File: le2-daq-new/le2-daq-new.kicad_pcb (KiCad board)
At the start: 2 copper layers, 161.3 x 88.4 mm, 11 parts, among them J1 PCIE_CONN, J2 PCIE_CONN, J3 PCIE_CONN, J4 PCIE_CONN, J5 Conn_01x02_Male, J6 TEST-POINT, J7 TEST-POINT, SW1 EN_HIGH, U1 ESP32-DEVKITC-32D

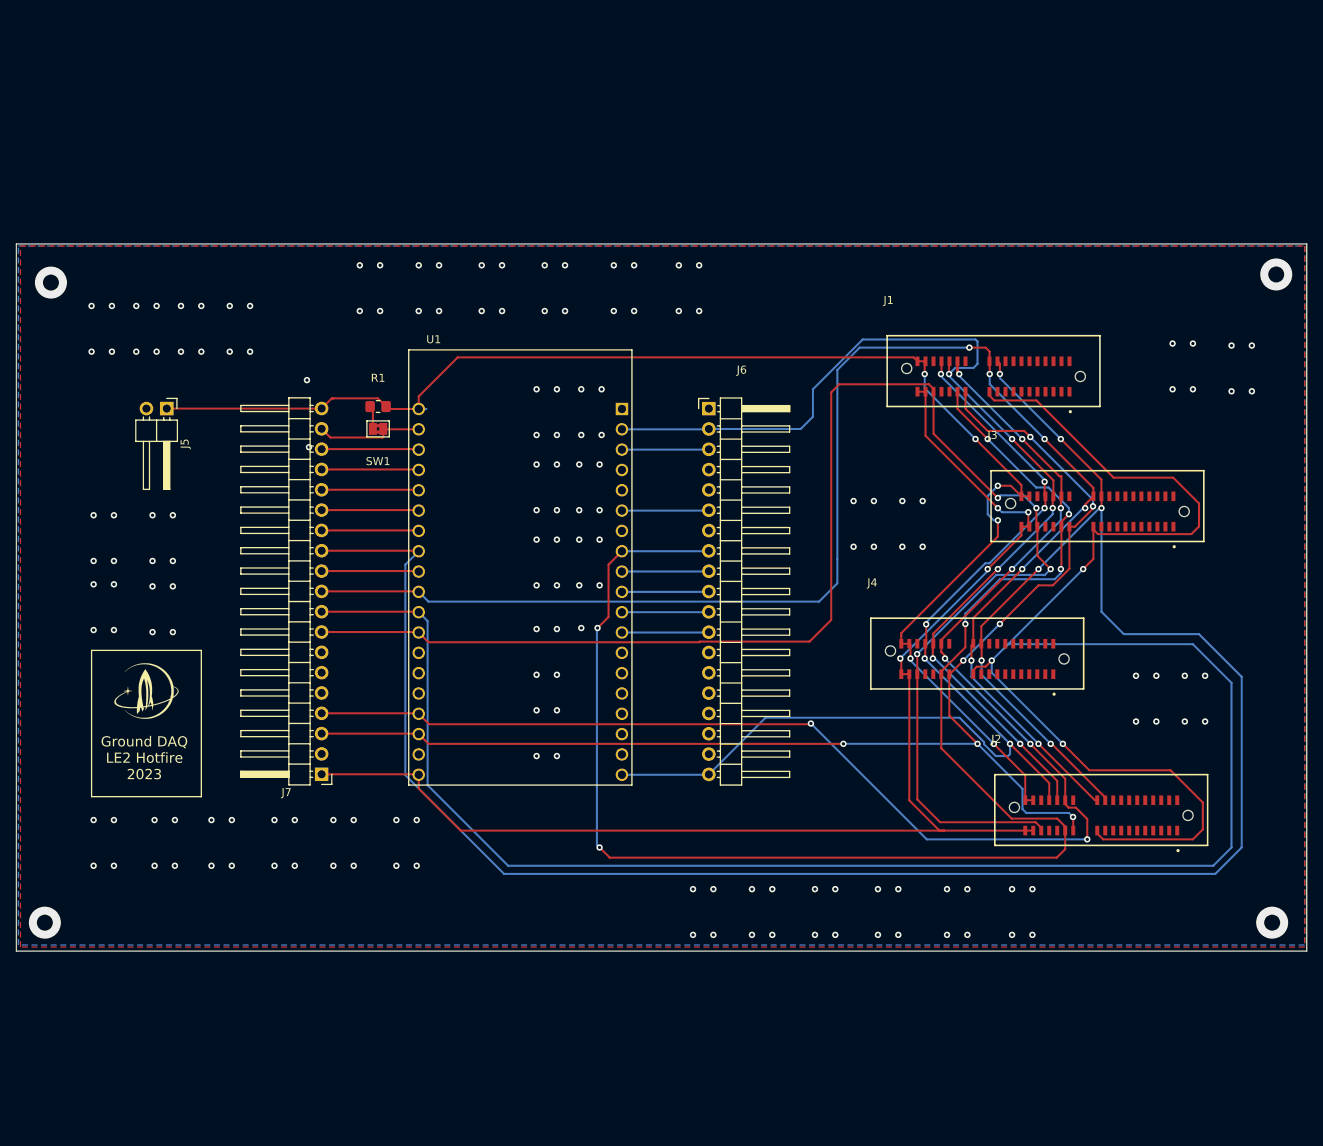
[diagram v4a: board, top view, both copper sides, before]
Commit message: new daq layout
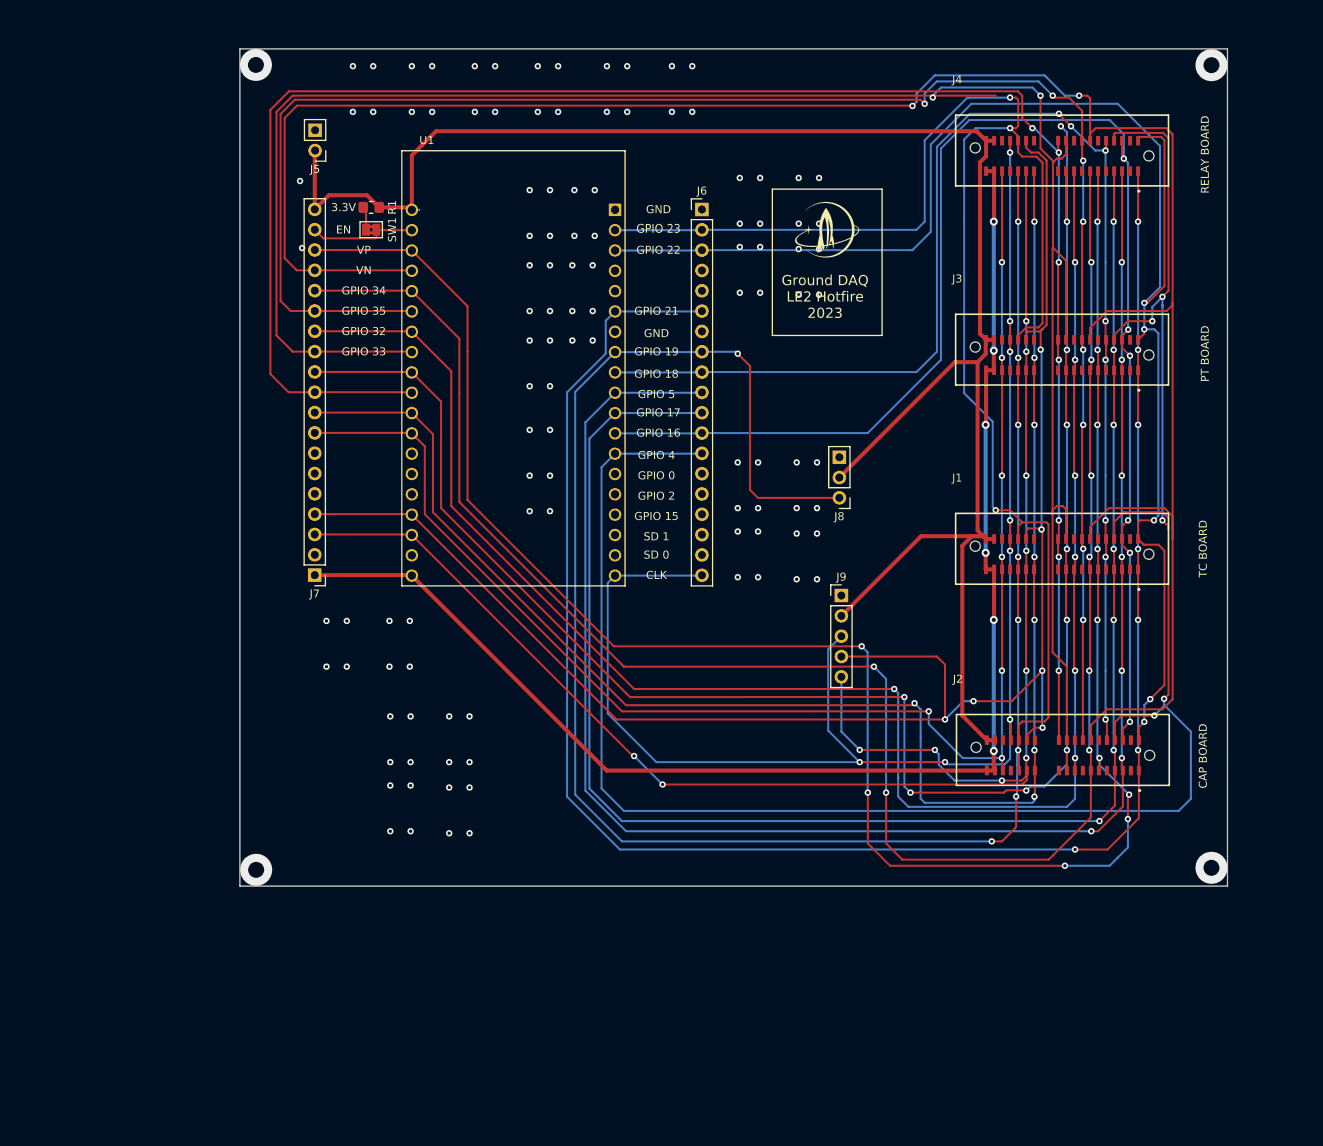
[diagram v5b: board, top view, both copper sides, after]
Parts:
- added J8: Conn_01x03_Male, Connector_PinHeader_2.54mm:PinHeader_1x03_P2.54mm_Vertical, F.Cu at (157.0, 89.4)
- added J9: Conn_01x05_Male, Connector_PinHeader_2.54mm:PinHeader_1x05_P2.54mm_Vertical, F.Cu at (157.2, 101.6)
- J5: value Conn_01x02_Male -> POWER; footprint Connector_PinHeader_2.54mm:PinHeader_1x02_P2.54mm_Horizontal -> Connector_PinHeader_2.54mm:PinHeader_1x02_P2.54mm_Vertical
- J6, J7: footprint Connector_PinHeader_2.54mm:PinHeader_1x19_P2.54mm_Horizontal -> Connector_PinHeader_2.54mm:PinHeader_1x19_P2.54mm_Vertical
- SW1: value EN_HIGH -> SW_Push
- moved G*** 102.8 mm to (155.4, 55.9)
- moved J4 63.8 mm to (184.8, 46.6)
- moved J5 37.2 mm to (91.4, 46.0), turned to 180 degrees
- moved J6 24.9 mm to (139.8, 53.4)
- moved SW1 24.9 mm to (98.5, 55.9)
- moved J7 24.9 mm to (91.4, 99.0)
- moved R1 24.9 mm to (98.5, 53.1)
- moved U1 24.9 mm to (116.2, 73.2)
- moved J1 23.8 mm to (184.8, 96.4)
- moved J3 20.1 mm to (184.8, 71.5)
- moved J2 8.91 mm to (184.9, 121.6)
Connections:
- J1 pad A01: (no net) -> RL SDA
- J1 pad A02: (no net) -> GND
- J1 pad A03: (no net) -> TC SDO
- J1 pad A04: (no net) -> TC SDI
- J1 pad A05: (no net) -> GND
- J1 pad A06: (no net) -> HX 1
- J1 pad A07: (no net) -> HX 3
- J1 pad A08: (no net) -> GND
- J1 pad A09: (no net) -> HX 5
- J1 pad A10: GND -> HX 7
- J1 pad A11: HX CLK -> GND
- J1 pad A12: CAP 2 -> HX CLK
- J1 pad A13: PHOTORES -> CAP 2
- J1 pad A14: GND -> PHOTORES
- J1 pad B01: (no net) -> RL SCL
- J1 pad B02: (no net) -> GND
- J1 pad B03: (no net) -> TC1 CS
- J1 pad B04: (no net) -> TC2 CS
- J1 pad B05: (no net) -> TC CLK
- J1 pad B06: (no net) -> GND
- J1 pad B07: (no net) -> HX 2
- J1 pad B08: (no net) -> HX 4
- J1 pad B09: (no net) -> GND
- J2 pad A01: (no net) -> RL SDA
- J2 pad A02: (no net) -> GND
- J2 pad A03: (no net) -> TC SDO
- J2 pad A04: (no net) -> TC SDI
- J2 pad A05: (no net) -> GND
- J2 pad A06: (no net) -> HX 1
- J2 pad A07: (no net) -> HX 3
- J2 pad A08: (no net) -> GND
- J2 pad A09: (no net) -> HX 5
- J2 pad A10: GND -> HX 7
- J2 pad A11: HX CLK -> GND
- J2 pad A12: CAP 2 -> HX CLK
- J2 pad A13: PHOTORES -> CAP 2
- J2 pad A14: GND -> PHOTORES
- J2 pad B01: (no net) -> RL SCL
- J2 pad B02: (no net) -> GND
- J2 pad B03: (no net) -> TC1 CS
- J2 pad B04: (no net) -> TC2 CS
- J2 pad B05: (no net) -> TC CLK
- J2 pad B06: (no net) -> GND
- J2 pad B07: (no net) -> HX 2
- J2 pad B08: (no net) -> HX 4
- J2 pad B09: (no net) -> GND
- J3 pad A01: (no net) -> RL SDA
- J3 pad A02: (no net) -> GND
- J3 pad A03: (no net) -> TC SDO
- J3 pad A04: (no net) -> TC SDI
- J3 pad A05: (no net) -> GND
- J3 pad A06: (no net) -> HX 1
- J3 pad A07: (no net) -> HX 3
- J3 pad A08: (no net) -> GND
- J3 pad A09: (no net) -> HX 5
- J3 pad A10: GND -> HX 7
- J3 pad A11: HX CLK -> GND
- J3 pad A12: CAP 2 -> HX CLK
- J3 pad A13: PHOTORES -> CAP 2
- J3 pad A14: GND -> PHOTORES
- J3 pad B01: (no net) -> RL SCL
- J3 pad B02: (no net) -> GND
- J3 pad B03: (no net) -> TC1 CS
- J3 pad B04: (no net) -> TC2 CS
- J3 pad B05: (no net) -> TC CLK
- J3 pad B06: (no net) -> GND
- J3 pad B07: (no net) -> HX 2
- J3 pad B08: (no net) -> HX 4
- J3 pad B09: (no net) -> GND
- J4 pad A01: (no net) -> RL SDA
- J4 pad A02: (no net) -> GND
- J4 pad A03: (no net) -> TC SDO
- J4 pad A04: (no net) -> TC SDI
- J4 pad A05: (no net) -> GND
- J4 pad A06: (no net) -> HX 1
- J4 pad A07: (no net) -> HX 3
- J4 pad A08: (no net) -> GND
- J4 pad A09: (no net) -> HX 5
- J4 pad A10: GND -> HX 7
- J4 pad A11: HX CLK -> GND
- J4 pad A12: CAP 2 -> HX CLK
- J4 pad A13: PHOTORES -> CAP 2
- J4 pad A14: GND -> PHOTORES
- J4 pad B01: (no net) -> RL SCL
- J4 pad B02: (no net) -> GND
- J4 pad B03: (no net) -> TC1 CS
- J4 pad B04: (no net) -> TC2 CS
- J4 pad B05: (no net) -> TC CLK
- J4 pad B06: (no net) -> GND
- J4 pad B07: (no net) -> HX 2
- J4 pad B08: (no net) -> HX 4
- J4 pad B09: (no net) -> GND
- J6 pad 10: TC1 CS -> TC SDO
- J6 pad 11: TC SDO -> TC SDI
- J6 pad 12: TC CLK -> TC1 CS
- J6 pad 13: unconnected-(J6-Pad13) -> TC2 CS
- J6 pad 9: TC2 CS -> TC CLK
- U1 pad 28: TC2 CS -> TC CLK
- U1 pad 29: TC1 CS -> TC SDO
- U1 pad 30: TC SDO -> TC SDI
- U1 pad 31: TC CLK -> TC1 CS
- U1 pad 32: unconnected-(U1-Pad32) -> TC2 CS
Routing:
- net HX 2: track 12.2 -> 269.2 mm, vias 0 -> 2
- net TC2 CS: track 10.9 -> 252.0 mm, vias 0 -> 5
- net HX 1: track 12.2 -> 250.7 mm, vias 0 -> 11
- net HX 3: track 12.2 -> 233.9 mm, vias 0 -> 8
- net RL SDA: track 10.9 -> 230.8 mm, vias 0 -> 7
- net HX 4: track 12.2 -> 223.9 mm, vias 0 -> 8
- net HX 7: track 12.2 -> 220.8 mm, vias 0 -> 10
- net TC SDI: track 0.00 -> 206.9 mm, vias 0 -> 7
- net HX 5: track 12.2 -> 218.1 mm, vias 0 -> 7
- net TC SDO: track 10.9 -> 212.3 mm, vias 0 -> 7
- net RL SCL: track 10.9 -> 193.8 mm, vias 0 -> 5
- net TC1 CS: track 10.9 -> 176.3 mm, vias 0 -> 6
- net TC CLK: track 10.9 -> 166.8 mm, vias 0 -> 8
- net HX CLK: track 318.1 -> 201.6 mm, vias 3 -> 8
- net RL INT: track 131.3 -> 192.7 mm, vias 6 -> 3
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- removed copper zone on B.Cu, net (none)
- removed copper zone on F.Cu, net GND
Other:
- board size 161.3 x 88.4 mm -> 123.4 x 104.6 mm
- board text added: "3.3V"
- board text added: "CAP BOARD"
- board text added: "CLK"
- board text added: "EN"
- board text added: "GND"
- board text added: "GPIO 0"
- board text added: "GPIO 15"
- board text added: "GPIO 16"
- board text added: "GPIO 17"
- board text added: "GPIO 18"
- board text added: "GPIO 19"
- board text added: "GPIO 2"
- board text added: "GPIO 21"
- board text added: "GPIO 22"
- board text added: "GPIO 23"
- board text added: "GPIO 32"
- board text added: "GPIO 33"
- board text added: "GPIO 34"
- board text added: "GPIO 35"
- board text added: "GPIO 4"
- board text added: "GPIO 5"
- board text added: "PT BOARD"
- board text added: "RELAY BOARD"
- board text added: "SD 0"
- board text added: "SD 1"
- board text added: "TC BOARD"
- board text added: "VN"
- board text added: "VP"
